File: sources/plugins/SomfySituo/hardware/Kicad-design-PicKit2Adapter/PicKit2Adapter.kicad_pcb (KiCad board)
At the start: 2 copper layers, 4 parts, among them J1 AVX 00-9188 006, P1 ICSP_PicKit2

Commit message: Finish PCB
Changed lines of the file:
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@@
     (effects (font (size 1.5 1.5) (thickness 0.3)))
   )
-  (gr_line (start 156.718 118.872) (end 156.718 111.76) (angle 90) (layer F.SilkS) (width 0.6))
-  (gr_line (start 152.146 111.76) (end 160.274 111.76) (angle 90) (layer F.SilkS) (width 0.6))
-  (gr_line (start 151.638 112.268) (end 152.146 111.76) (angle 90) (layer F.SilkS) (width 0.6))
-  (gr_line (start 151.638 114.808) (end 151.638 112.268) (angle 90) (layer F.SilkS) (width 0.6))
-  (gr_line (start 152.146 115.316) (end 151.638 114.808) (angle 90) (layer F.SilkS) (width 0.6))
-  (gr_line (start 155.194 115.316) (end 152.146 115.316) (angle 90) (layer F.SilkS) (width 0.6))
-  (gr_line (start 155.702 115.824) (end 155.194 115.316) (angle 90) (layer F.SilkS) (width 0.6))
-  (gr_line (start 155.702 118.364) (end 155.702 115.824) (angle 90) (layer F.SilkS) (width 0.6))
-  (gr_line (start 155.194 118.872) (end 155.702 118.364) (angle 90) (layer F.SilkS) (width 0.6))
-  (gr_line (start 151.638 118.872) (end 155.194 118.872) (angle 90) (layer F.SilkS) (width 0.6))
+  (gr_line (start 137.414 122.428) (end 137.414 115.316) (angle 90) (layer F.SilkS) (width 0.6))
+  (gr_line (start 132.842 115.316) (end 140.97 115.316) (angle 90) (layer F.SilkS) (width 0.6))
+  (gr_line (start 132.334 115.824) (end 132.842 115.316) (angle 90) (layer F.SilkS) (width 0.6))
+  (gr_line (start 132.334 118.364) (end 132.334 115.824) (angle 90) (layer F.SilkS) (width 0.6))
+  (gr_line (start 132.842 118.872) (end 132.334 118.364) (angle 90) (layer F.SilkS) (width 0.6))
+  (gr_line (start 135.89 118.872) (end 132.842 118.872) (angle 90) (layer F.SilkS) (width 0.6))
+  (gr_line (start 136.398 119.38) (end 135.89 118.872) (angle 90) (layer F.SilkS) (width 0.6))
+  (gr_line (start 136.398 121.92) (end 136.398 119.38) (angle 90) (layer F.SilkS) (width 0.6))
+  (gr_line (start 135.89 122.428) (end 136.398 121.92) (angle 90) (layer F.SilkS) (width 0.6))
+  (gr_line (start 132.334 122.428) (end 135.89 122.428) (angle 90) (layer F.SilkS) (width 0.6))
   (gr_text "Pickit2 ICSP\nadapter" (at 136.652 111.252) (layer F.SilkS)
     (effects (font (size 1.5 1.5) (thickness 0.3)))

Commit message: Send PCB to factoring
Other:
- board outline added: 40.1 x 17.8 mm

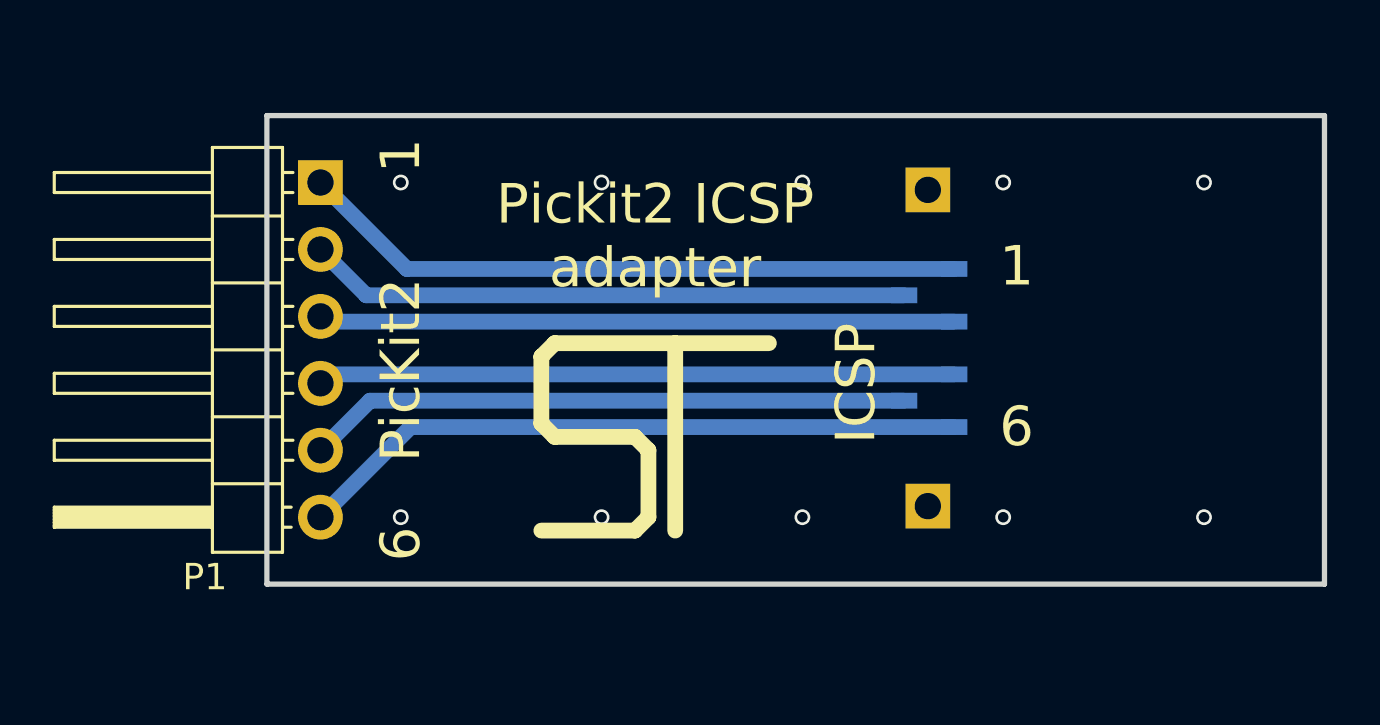
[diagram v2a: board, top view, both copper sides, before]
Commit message: Add 4-pins and 8-pins connectors on ICSP adapter
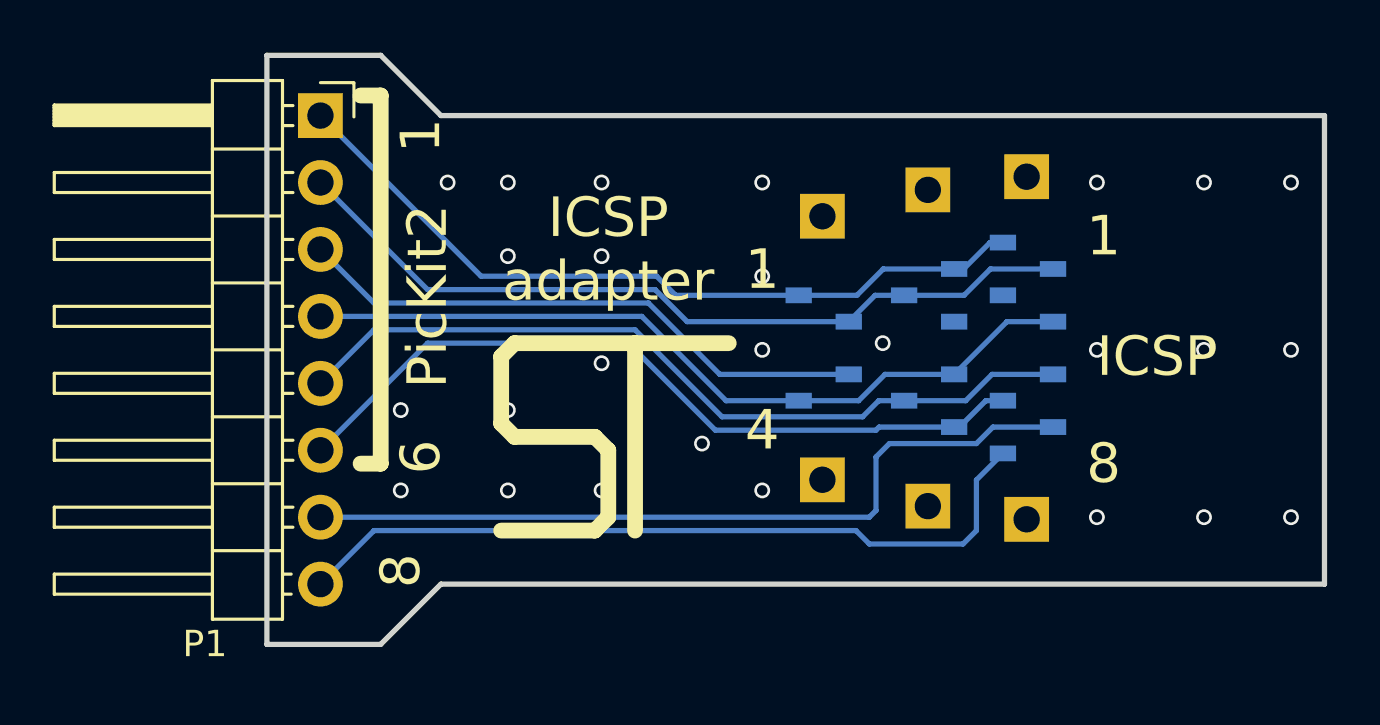
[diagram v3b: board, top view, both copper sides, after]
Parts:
- added J2: AVX 00-9188 004, AVX 00-9188 006:AVX_00-9188_004, B.Cu at (144.0, 112.5)
- added J3: AVX 00-9188 008, AVX 00-9188 006:AVX_00-9188_008, B.Cu at (151.8, 112.5)
- added REF**: Pin_Header_Straight_1x01_Pitch2.54mm, Pin_Headers:Pin_Header_Straight_1x01_Pitch2.54mm, B.Cu at (143.0, 110.5)
- added REF**: Pin_Header_Straight_1x01_Pitch2.54mm, Pin_Headers:Pin_Header_Straight_1x01_Pitch2.54mm, B.Cu at (143.0, 120.5)
- added REF**: Pin_Header_Straight_1x01_Pitch2.54mm, Pin_Headers:Pin_Header_Straight_1x01_Pitch2.54mm, B.Cu at (150.8, 122.0)
- added REF**: Pin_Header_Straight_1x01_Pitch2.54mm, Pin_Headers:Pin_Header_Straight_1x01_Pitch2.54mm, B.Cu at (150.8, 109.0)
- P1: value ICSP_PicKit2 -> Conn_01x08; footprint Pin_Headers:Pin_Header_Angled_1x06_Pitch2.54mm -> Pin_Headers:Pin_Header_Angled_1x08_Pitch2.54mm
- moved P1 2.54 mm to (124.0, 124.5)
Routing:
- net Net-(J3-Pad7): track 0.00 -> 30.4 mm
- net Net-(J3-Pad8): track 0.00 -> 29.5 mm
- net Net-(J1-Pad2): track 22.9 -> 30.8 mm
- net Net-(J1-Pad5): track 22.9 -> 30.7 mm
- net Net-(J1-Pad4): track 24.2 -> 30.4 mm
- net Net-(J1-Pad6): track 25.5 -> 29.4 mm
- net Net-(J1-Pad1): track 25.4 -> 29.2 mm
- net GND: track 24.1 -> 22.0 mm, vias 0 -> 26
- net (no net): vias 10 -> 0
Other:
- board size 40.1 x 17.8 mm -> 40.1 x 22.4 mm
- net class Default: trace_width 0.6 -> 0.2
- board text added: "4"
- board text added: "8"
- board text added: "ICSP adapter"
- board text removed: "Pickit2 ICSP adapter"
